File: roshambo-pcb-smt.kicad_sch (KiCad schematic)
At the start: 49 parts, among them J1 Conn_01x06_Socket, J2 Conn_01x03_Pin, J3 Conn_01x03_Pin, Q1 2N7002, Q2 2N7002, Q3 2N7002, Q4 2N7002, Q5 2N7002, Q6 2N7002, Q7 2N7002, Q8 2N7002, Q9 2N7002, U1 Pico

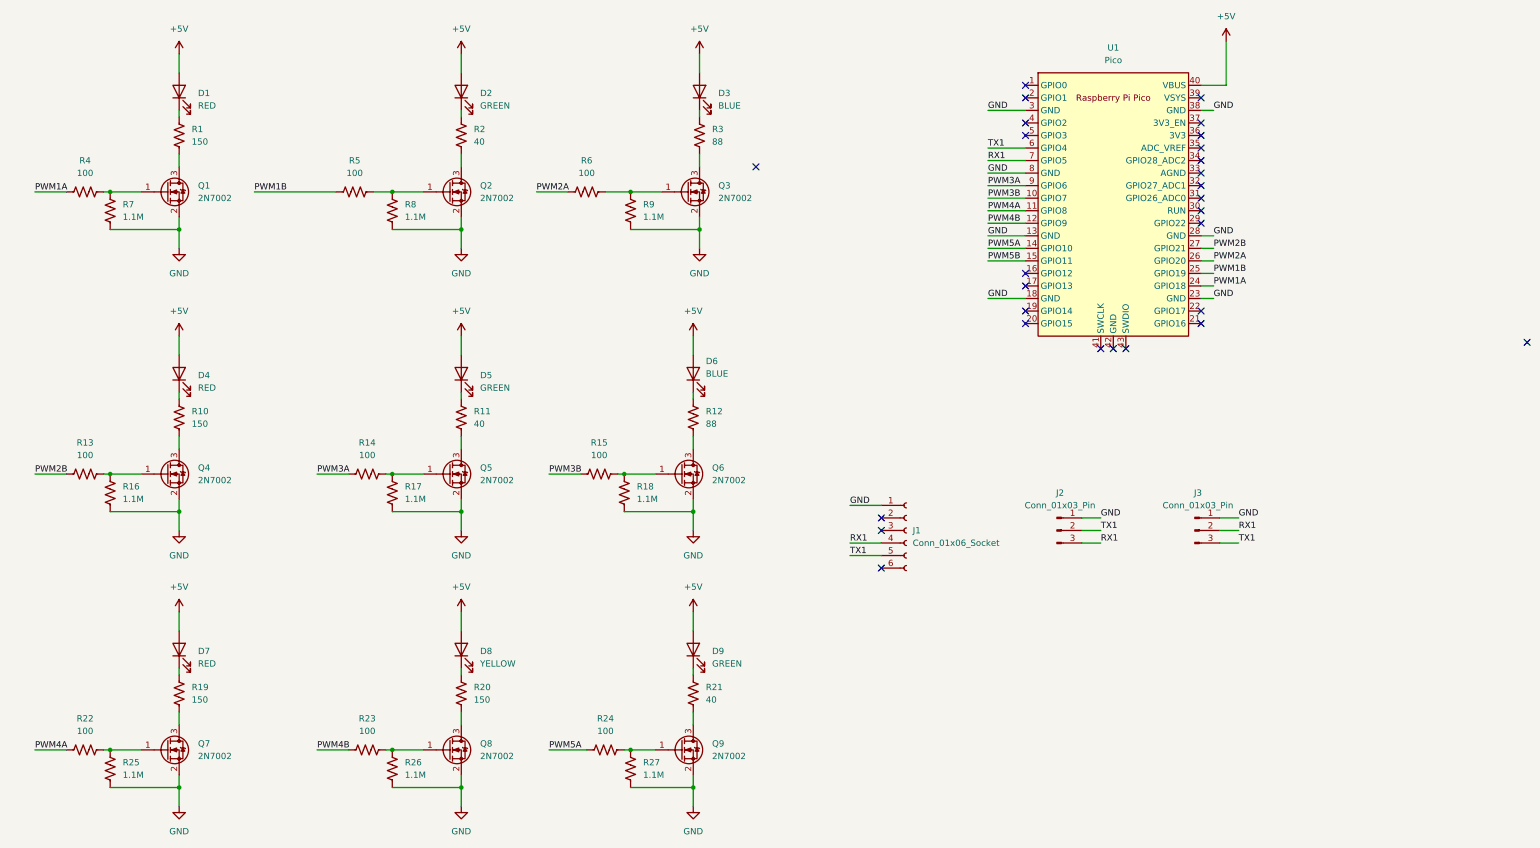
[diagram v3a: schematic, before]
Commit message: Get a PDF version of the schematic
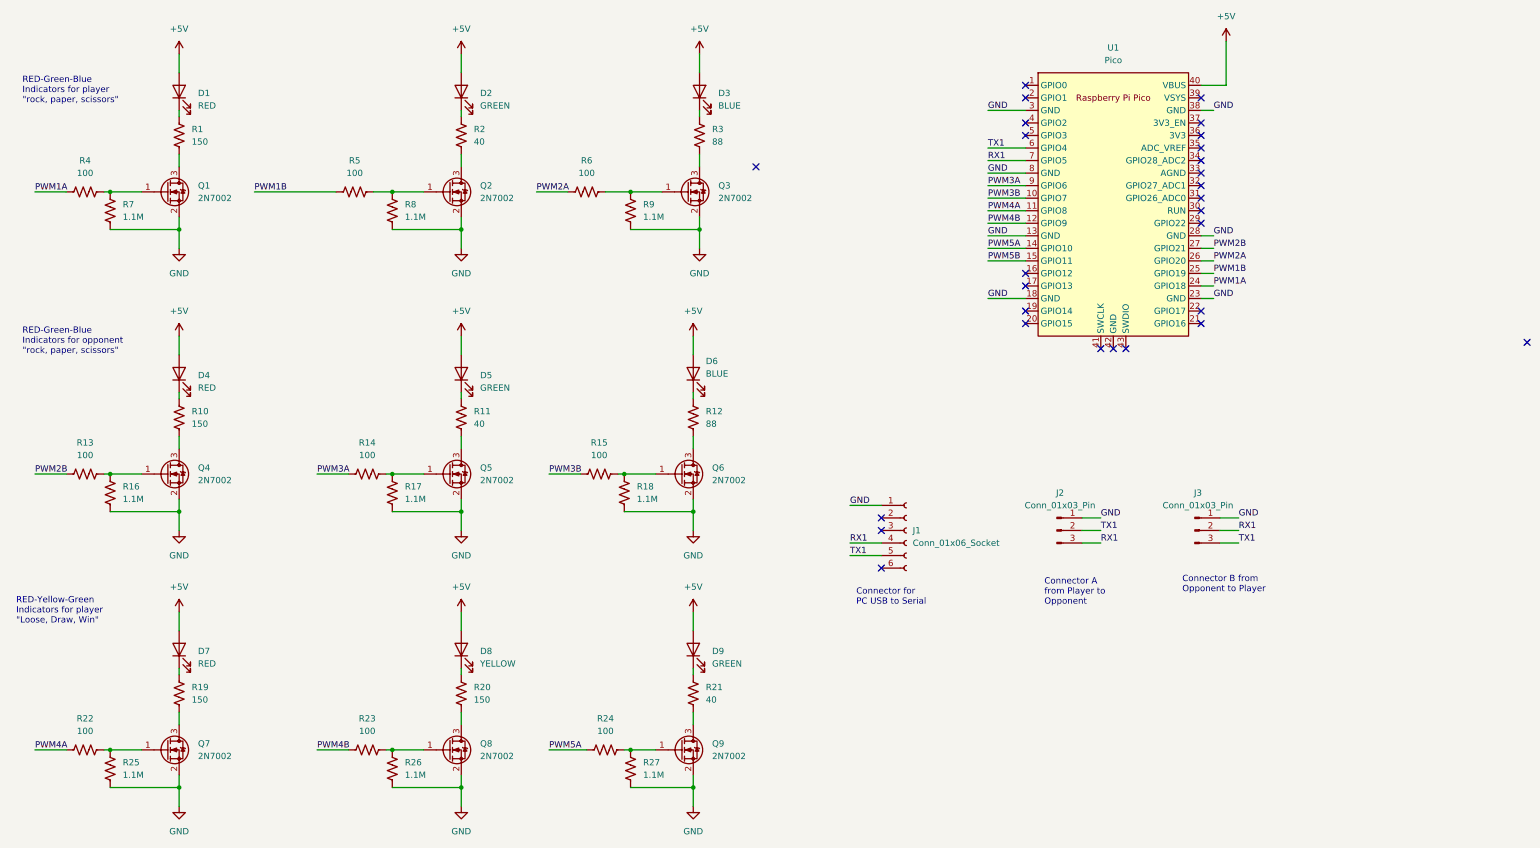
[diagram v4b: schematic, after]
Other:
- note added: "Connector A from Player to Opponent"
- note added: "Connector B from Opponent to Player"
- note added: "Connector for PC USB to Serial"
- note added: "RED-Green-Blue Indicators for opponent "rock, paper, scissors""
- note added: "RED-Green-Blue Indicators for player "rock, paper, scissors""
- note added: "RED-Yellow-Green Indicators for player "Loose, Draw, Win""
- company: (none) -> Ludwig Makerspace
- title: (none) -> Robot Roshambo SMT
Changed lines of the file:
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@@
 (kicad_sch (version 20230121) (generator eeschema)
   (paper "A4")
+  (title_block
+    (title "Robot Roshambo SMT")
+    (rev "v0.1")
+    (company "Ludwig Makerspace")
+  )
   (junction (at 140.97 166.37) (diameter 0) (color 0 0 0 0)
   )
@@
     (stroke (width 0) (type default))
   )
+  (text "RED-Green-Blue\nIndicators for player \n\"rock, paper, scissors\"\n"
+    (at 17.78 35.56 0)
+    (effects (font (size 1.27 1.27)) (justify left bottom))
+  )
+  (text "Connector A\nfrom Player to \nOpponent" (at 224.79 137.16 0)
+    (effects (font (size 1.27 1.27)) (justify left bottom))
+  )
+  (text "RED-Yellow-Green\nIndicators for player \n\"Loose, Draw, Win\"\n"
+    (at 16.51 140.97 0)
+    (effects (font (size 1.27 1.27)) (justify left bottom))
+  )
+  (text "Connector for \nPC USB to Serial \n" (at 186.69 137.16 0)
+    (effects (font (size 1.27 1.27)) (justify left bottom))
+  )
+  (text "Connector B from\nOpponent to Player\n" (at 252.73 134.62 0)
+    (effects (font (size 1.27 1.27)) (justify left bottom))
+  )
+  (text "RED-Green-Blue\nIndicators for opponent \n\"rock, paper, scissors\"\n"
+    (at 17.78 86.36 0)
+    (effects (font (size 1.27 1.27)) (justify left bottom))
+  )
   (label "GND" (at 264.16 119.38 0) (fields_autoplaced)

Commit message: use 595 shift registers
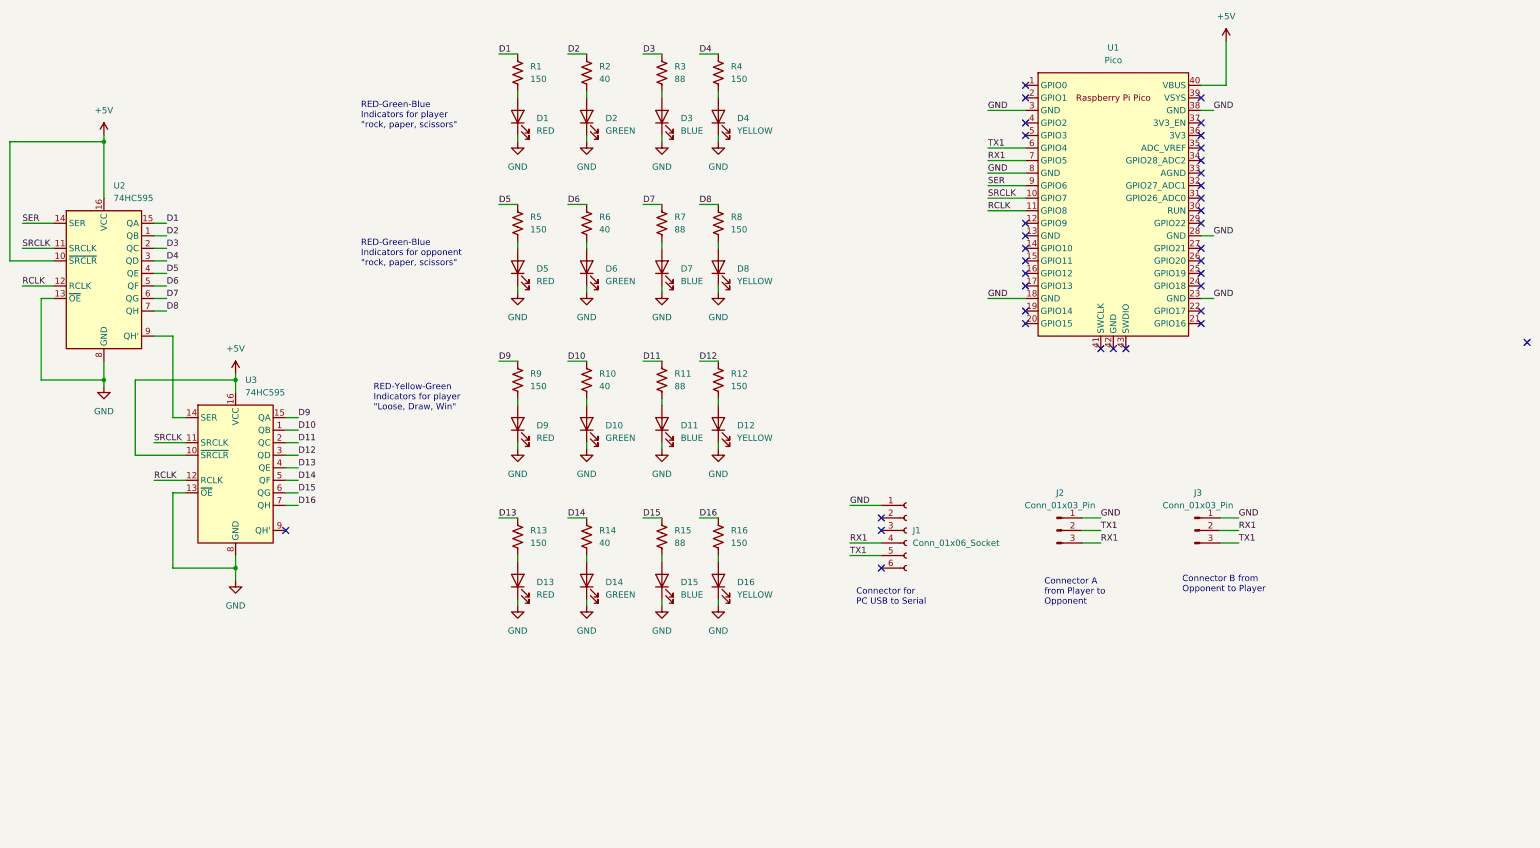
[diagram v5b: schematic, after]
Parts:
- removed Q1, Q2, Q3, Q4, Q5, Q6, Q7, Q8, Q9: 2N7002, Package_TO_SOT_SMD:SOT-23, symbol Transistor_FET:2N7002
- removed R17, R18, R25, R26, R27: 1.1M, Resistor_SMD:R_0402_1005Metric, symbol Device:R_US
- removed R19, R20: 150, Resistor_SMD:R_0402_1005Metric, symbol Device:R_US
- removed R21: 40, Resistor_SMD:R_0402_1005Metric, symbol Device:R_US
- removed R22, R23, R24: 100, Resistor_SMD:R_0402_1005Metric, symbol Device:R_US
- added D10, D14: GREEN, LED_SMD:LED_0603_1608Metric, symbol Device:LED
- added D11, D15: BLUE, LED_SMD:LED_0603_1608Metric, symbol Device:LED
- added D12, D16: YELLOW, LED_SMD:LED_0603_1608Metric, symbol Device:LED
- added D13: RED, LED_SMD:LED_0603_1608Metric, symbol Device:LED
- added U2, U3: 74HC595, Package_SO:SO-16_3.9x9.9mm_P1.27mm, symbol 74xx:74HC595
- D4: value RED -> YELLOW
- D5, D9: value GREEN -> RED
- D6: value BLUE -> GREEN
- D7: value RED -> BLUE
- R10: value 150 -> 40
- R11: value 40 -> 88
- R12: value 88 -> 150
- R13, R4, R5: value 100 -> 150
- R14, R6: value 100 -> 40
- R15: value 100 -> 88
- R16, R8, R9: value 1.1M -> 150
- R7: value 1.1M -> 88
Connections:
- net +5V: now also U2.10 (~{SRCLR}), U2.16 (VCC), U3.10 (~{SRCLR}), U3.16 (VCC); no longer D1.2 (A), D2.2 (A), D3.2 (A), D4.2 (A), D5.2 (A), D6.2 (A), D7.2 (A), D8.2 (A), D9.2 (A)
- net GND: now also D1.1 (K), D2.1 (K), D3.1 (K), D4.1 (K), D5.1 (K), D6.1 (K), D7.1 (K), D8.1 (K), D9.1 (K), D10.1 (K), D11.1 (K), D12.1 (K), D13.1 (K), D14.1 (K), D15.1 (K), D16.1 (K), U2.13 (~{OE}), U2.8 (GND), U3.13 (~{OE}), U3.8 (GND); no longer R16.2, R7.2, R8.2, R9.2, U1.13 (GND)
- net at R15.2: now also D15.2 (A)
- net D12: now reaches R12.1
- net D12: now also U3.3 (QD); no longer D6.1 (K)
- net D10: now reaches R10.1
- net D10: now also U3.1 (QB); no longer D4.1 (K)
- net D11: now reaches R11.1
- net D11: now also U3.2 (QC); no longer D5.1 (K)
- net at R4.2: now also D4.2 (A); no longer R7.1
- net at R6.2: now also D6.2 (A); no longer R9.1
- net at R14.2: now also D14.2 (A)
- net D3: now reaches R3.1
- net D3: now also U2.2 (QC); no longer D3.1 (K)
- net at R3.2: now also D3.2 (A)
- net at R5.2: now also D5.2 (A); no longer R8.1
- net D2: now reaches R2.1
- net D2: now also U2.1 (QB); no longer D2.1 (K)
- net at R2.2: now also D2.2 (A)
- net at R11.2: now also D11.2 (A)
- net at R13.2: now also D13.2 (A); no longer R16.1
- net at R12.2: now also D12.2 (A)
- net at R10.2: now also D10.2 (A)
- net at R1.2: now also D1.2 (A)
- net D1: now reaches R1.1
- net D1: now also U2.15 (QA); no longer D1.1 (K)
- net PWM1A: no longer names the net of U1.24 (GPIO18)
- net PWM1A: no longer R4.1
- net PWM1B: no longer names the net of U1.25 (GPIO19)
- net PWM1B: no longer R5.1
- net PWM2A: no longer names the net of U1.26 (GPIO20)
- net PWM2A: no longer R6.1
- net PWM2B: no longer names the net of U1.27 (GPIO21)
- net PWM2B: no longer R13.1
- net PWM3A renamed D14
- net D14: now also U3.5 (QF); no longer U1.9 (GPIO6)
- net PWM3B renamed D15
- net D15: now also U3.6 (QG); no longer U1.10 (GPIO7)
- net PWM4A renamed RCLK
- net RCLK: now also U2.12 (RCLK), U3.12 (RCLK)
- net PWM4B: no longer names the net of U1.12 (GPIO9)
- net PWM5A: no longer names the net of U1.14 (GPIO10)
- net PWM5B: no longer names the net of U1.15 (GPIO11)
- new net: U2.9 (QH'), U3.14 (SER)
- new net: D7.2 (A), R7.2
- new net: D8.2 (A), R8.2
- new net: D16.2 (A), R16.2
- new net: D9.2 (A), R9.2
- new net D13: R13.1, U3.4 (QE)
- new net D16: R16.1, U3.7 (QH)
- new net D4: R4.1, U2.3 (QD)
- new net D5: R5.1, U2.4 (QE)
- new net D6: R6.1, U2.5 (QF)
- new net D7: R7.1, U2.6 (QG)
- new net D8: R8.1, U2.7 (QH)
- new net D9: R9.1, U3.15 (QA)
- new net SER: U1.9 (GPIO6), U2.14 (SER)
- new net SRCLK: U1.10 (GPIO7), U2.11 (SRCLK), U3.11 (SRCLK)
- no-connect marks 28 -> 36
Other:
- moved on the sheet: D1, D2, D3, R1, R2, R3

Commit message: Add reset switch, OE
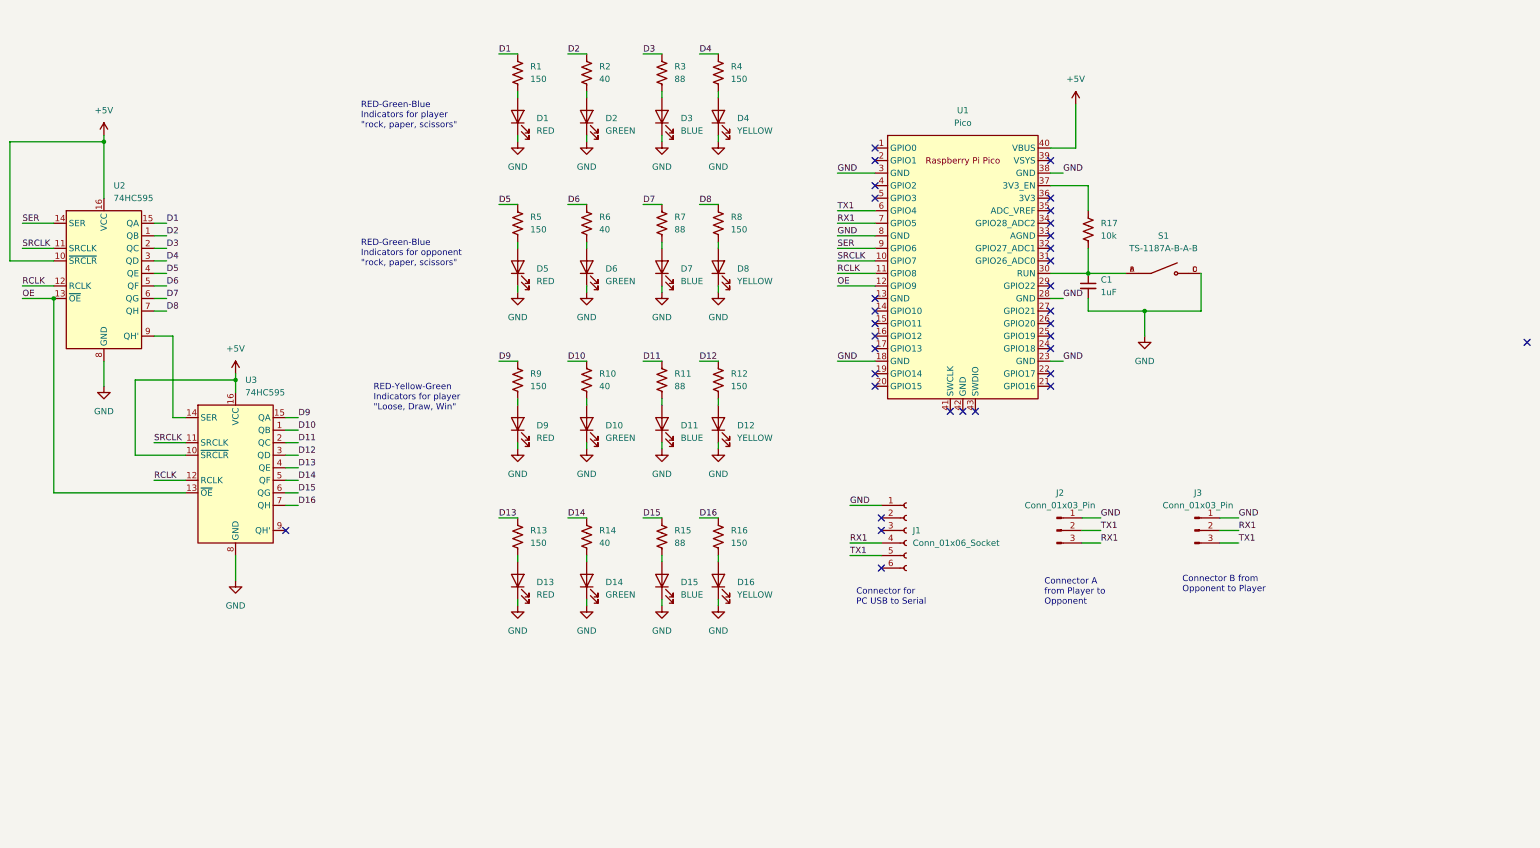
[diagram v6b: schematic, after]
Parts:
- added C1: 1uF, Capacitor_SMD:C_0603_1608Metric, symbol Device:C_Small
- added R17: 10k, Resistor_SMD:R_0402_1005Metric, symbol Device:R_US
- added S1: TS-1187A-B-A-B, TS-1187A-B-A-B:SW_TS-1187A-B-A-B, symbol TS-1187A-B-A-B:TS-1187A-B-A-B
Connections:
- net GND: now also C1.2, S1.C, S1.D; no longer U2.13 (~{OE}), U3.13 (~{OE})
- net OE: now reaches U1.12 (GPIO9)
- net OE: now also U2.13 (~{OE}), U3.13 (~{OE})
- net at U1.30 (RUN): now also C1.1, R17.2, S1.A, S1.B
- net at U1.37 (3V3_EN): now also R17.1
- no-connect marks 36 -> 33
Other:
- moved on the sheet: U1
